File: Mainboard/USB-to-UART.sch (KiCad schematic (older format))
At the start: 8 parts, among them U9 CH340B

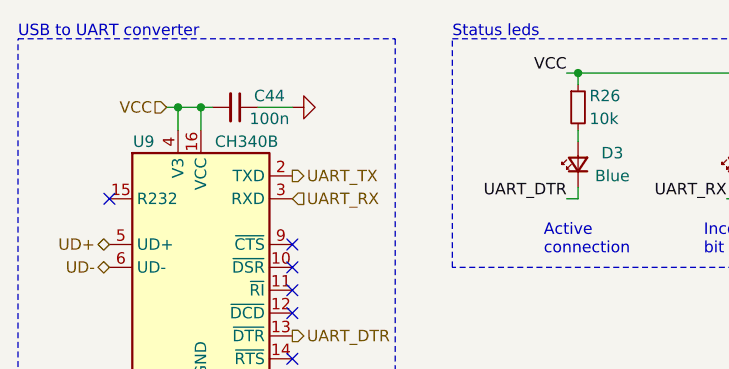
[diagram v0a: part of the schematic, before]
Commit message: Before testing CH340B and VCHG
Cleaned up amp lay-out a bit in the meanwhile
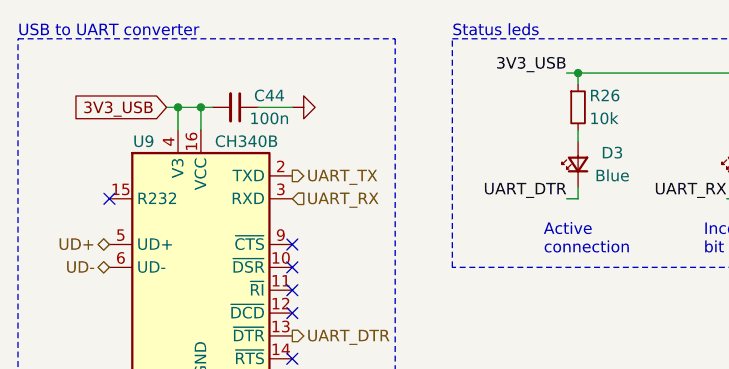
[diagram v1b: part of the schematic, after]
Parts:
- C44: Manufacturer Walsin -> Murata; Partnumber 0603B104J500CT -> GCM188L81H104KA57D
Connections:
- net VCC renamed 3V3_USB
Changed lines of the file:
@@
 $Descr A4 11693 8268
 encoding utf-8
-Sheet 2 9
+Sheet 10 11
 Title "4x38W amp with DSP and BT"
-Date "2021-11-08"
+Date "2021-11-19"
 Rev "0.2"
 Comp "ZOUDIO"
@@
 F 2 "Capacitor_SMD:C_0603_1608Metric" H 4950 3100 50  0001 C CNN
 F 3 "~" H 4950 3100 50  0001 C CNN
-F 4 "Walsin" H 4950 3100 50  0001 C CNN "Manufacturer"
-F 5 "0603B104J500CT" H 4950 3100 50  0001 C CNN "Partnumber"
+F 4 "Murata" H 4950 3100 50  0001 C CNN "Manufacturer"
+F 5 "GCM188L81H104KA57D" H 4950 3100 50  0001 C CNN "Partnumber"
 	1    4950 3100
 	0    1    1    0
@@
 Wire Wire Line
 	4650 3100 4700 3100
-Text HLabel 4650 3100 0    50   Input ~ 0
-VCC
 Connection ~ 4700 3100
 Wire Wire Line
 	6450 2950 6400 2950
-Text Label 6400 2950 2    50   ~ 0
-VCC
 Text Label 6400 3500 2    50   ~ 0
 UART_DTR
@@
 	8100 3800 5900 3800
 $Comp
-L power:GND #PWR?
+L power:GND #PWR0162
 U 1 1 61ADB0CE
 P 4800 4450
-F 0 "#PWR?" H 4800 4200 50  0001 C CNN
+F 0 "#PWR0162" H 4800 4200 50  0001 C CNN
 F 1 "GND" H 4800 4300 50  0000 C CNN
 F 2 "" H 4800 4450 50  0001 C CNN
@@
 	1    0    0    -1
 $EndComp
+Text GLabel 4650 3100 0    50   Input ~ 0
+3V3_USB
+Text Label 6400 2950 2    50   ~ 0
+3V3_USB
 $EndSCHEMATC

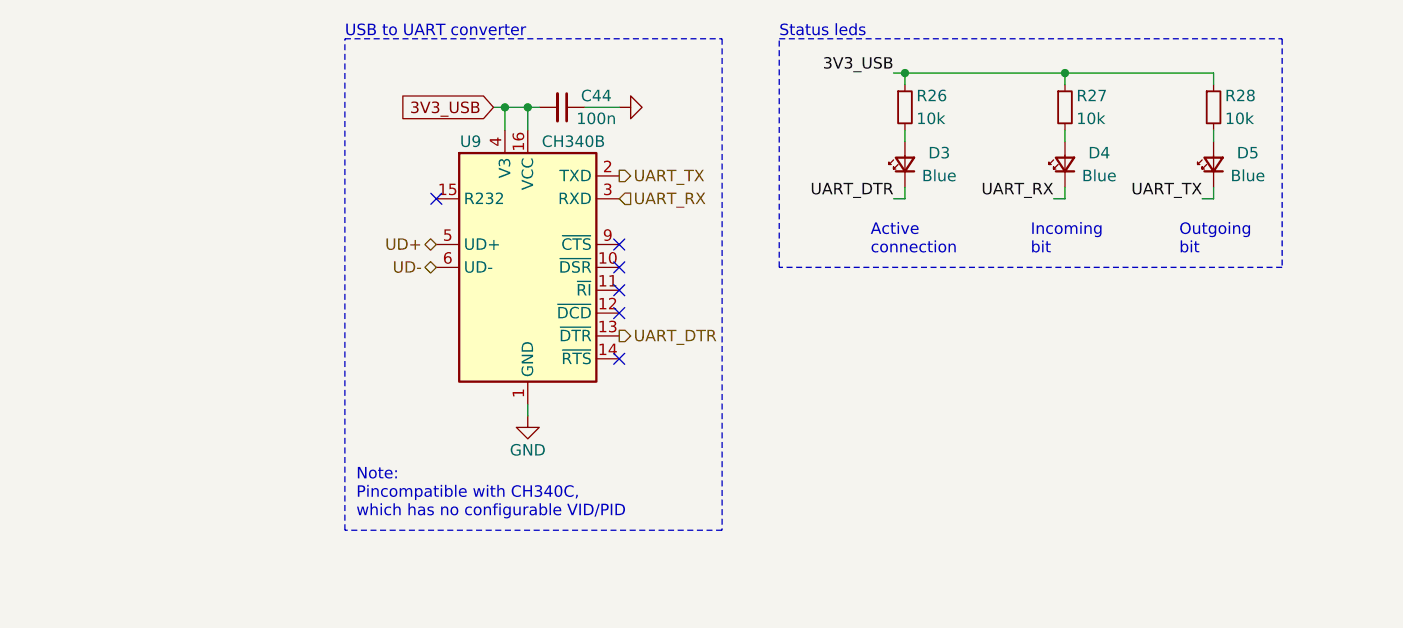
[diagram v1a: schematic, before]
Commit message: Result after weekend of lay-out
Pretty far, just neats to be cleaned up for production.
Does not pass DRC yet.
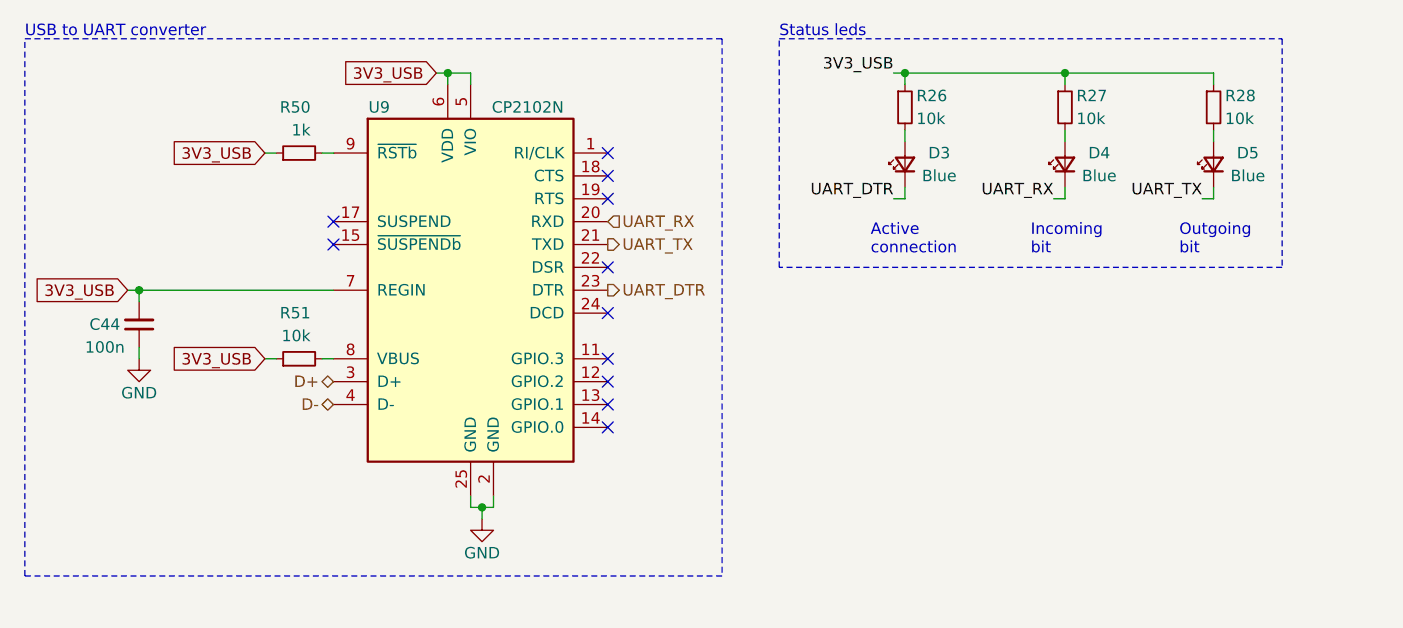
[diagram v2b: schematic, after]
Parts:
- removed U9: CH340B, Package_SO:SOIC-16_3.9x9.9mm_P1.27mm, symbol Interface_USB:CH340C
- added R50: 1k, Resistor_SMD:R_0603_1608Metric, symbol Device:R_Small
- added R51: 10k, Resistor_SMD:R_0603_1608Metric, symbol Device:R_Small
- added U9: CP2102N, Package_DFN_QFN:QFN-24-1EP_4x4mm_P0.5mm_EP2.6x2.6mm, symbol Interface_USB:CP2102N-A01-GQFN24
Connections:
- net 3V3_USB: now also R50.1, R51.1, U9.5 (VIO), U9.6 (VDD), U9.7 (REGIN)
- net GND: now also U9.2 (GND), U9.25 (GND)
- net UART_DTR: now also U9.23 (DTR)
- net UART_RX: now also U9.20 (RXD)
- net UART_TX: now also U9.21 (TXD)
- new net: R51.2, U9.8 (VBUS)
- new net: R50.2, U9.9 (~RSTb)
- new net D+: U9.3 (D+)
- new net D-: U9.4 (D-)
- no-connect marks 6 -> 11
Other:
- note removed: "Note:\nPincompatible with CH340C,\nwhich has no configurable VID/PID"
- moved on the sheet: C44
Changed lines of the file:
@@
 Comment4 ""
 $EndDescr
-$Comp
-L power:GND #PWR?
-U 1 1 5FD85D4B
-P 5200 3100
-AR Path="/5FD85D4B" Ref="#PWR?"  Part="1"
-AR Path="/5FD15AD6/5FD85D4B" Ref="#PWR?"  Part="1"
-AR Path="/5FBDE62F/5FD85D4B" Ref="#PWR?"  Part="1"
-AR Path="/5FD81784/5FD85D4B" Ref="#PWR?"  Part="1"
-AR Path="/5FCDB1AE/5FD85D4B" Ref="#PWR?"  Part="1"
-AR Path="/5FF9E05B/5FD85D4B" Ref="#PWR?"  Part="1"
-AR Path="/60A7E145/5FD85D4B" Ref="#PWR0186"  Part="1"
-F 0 "#PWR0186" H 5200 2850 50  0001 C CNN
-F 1 "GND" H 5205 2927 50  0001 C CNN
-F 2 "" H 5200 3100 50  0001 C CNN
-F 3 "" H 5200 3100 50  0001 C CNN
-	1    5200 3100
-	0    -1   -1   0
-$EndComp
-Text HLabel 5200 4100 2    50   Output ~ 0
+Text HLabel 5150 3900 2    50   Output ~ 0
 UART_DTR
 Wire Notes Line
-	5650 4950 4000 4950
-Wire Notes Line
-	4000 4950 4000 2800
-Text HLabel 4400 3700 0    50   BiDi ~ 0
-UD+
-Text HLabel 4400 3800 0    50   BiDi ~ 0
-UD-
+	5650 5150 2600 5150
+Wire Notes Line
+	2600 5150 2600 2800
+Text HLabel 3950 4300 0    50   BiDi ~ 0
+D+
+Text HLabel 3950 4400 0    50   BiDi ~ 0
+D-
 $Comp
 L Device:C_Small C?
 U 1 1 5FD85D40
-P 4950 3100
+P 3100 4050
 AR Path="/5FD85D40" Ref="C?"  Part="1"
 AR Path="/5FCC1D27/5FD85D40" Ref="C?"  Part="1"
@@
 AR Path="/5FF9E05B/5FD85D40" Ref="C?"  Part="1"
 AR Path="/60A7E145/5FD85D40" Ref="C44"  Part="1"
-F 0 "C44" V 4900 3250 50  0000 C CNN
-F 1 "100n" V 5000 3250 50  0000 C CNN
-F 2 "Capacitor_SMD:C_0603_1608Metric" H 4950 3100 50  0001 C CNN
-F 3 "~" H 4950 3100 50  0001 C CNN
-F 4 "Murata" H 4950 3100 50  0001 C CNN "Manufacturer"
-F 5 "GCM188L81H104KA57D" H 4950 3100 50  0001 C CNN "Partnumber"
-	1    4950 3100
-	0    1    1    0
-$EndComp
-Wire Wire Line
-	5200 3100 5050 3100
-Wire Wire Line
-	4850 3100 4800 3100
-Wire Wire Line
-	4700 3200 4700 3100
-Wire Wire Line
-	4700 3100 4800 3100
-Connection ~ 4800 3100
-Wire Wire Line
-	4800 3100 4800 3200
-NoConn ~ 4400 3500
-NoConn ~ 5200 3700
-NoConn ~ 5200 3800
-NoConn ~ 5200 3900
-NoConn ~ 5200 4000
-NoConn ~ 5200 4200
-Wire Wire Line
-	4800 4400 4800 4450
-$Comp
-L Interface_USB:CH340C U9
-U 1 1 60B2C7AB
-P 4800 3800
-F 0 "U9" H 4550 4350 50  0000 C CNN
-F 1 "CH340B" H 5000 4350 50  0000 C CNN
-F 2 "Package_SO:SOIC-16_3.9x9.9mm_P1.27mm" H 4850 3250 50  0001 L CNN
-F 3 "~" H 4450 4600 50  0001 C CNN
-	1    4800 3800
-	1    0    0    -1
-$EndComp
-Text Notes 4050 4900 0    50   ~ 0
-Note:\nPincompatible with CH340C,\nwhich has no configurable VID/PID
-Text Notes 4000 2800 0    50   ~ 0
+F 0 "C44" H 2950 4050 50  0000 C CNN
+F 1 "100n" H 2950 4150 50  0000 C CNN
+F 2 "Capacitor_SMD:C_0603_1608Metric" H 3100 4050 50  0001 C CNN
+F 3 "~" H 3100 4050 50  0001 C CNN
+F 4 "Murata" H 3100 4050 50  0001 C CNN "Manufacturer"
+F 5 "GCM188L81H104KA57D" H 3100 4050 50  0001 C CNN "Partnumber"
+	1    3100 4050
+	1    0    0    1
+$EndComp
+Text Notes 2600 2800 0    50   ~ 0
 USB to UART converter
-Wire Notes Line
-	4000 2800 5650 2800
-Text HLabel 5200 3500 2    50   Input ~ 0
+Text HLabel 5150 3600 2    50   Input ~ 0
 UART_RX
-Text HLabel 5200 3400 2    50   Output ~ 0
+Text HLabel 5150 3700 2    50   Output ~ 0
 UART_TX
 Wire Notes Line
-	5650 2800 5650 4950
+	5650 2800 5650 5150
 Text Notes 5900 2800 0    50   ~ 0
 Status leds
@@
 $EndComp
 Wire Wire Line
-	4650 3100 4700 3100
-Connection ~ 4700 3100
-Wire Wire Line
 	6450 2950 6400 2950
 Text Label 6400 3500 2    50   ~ 0
@@
 Wire Notes Line
 	8100 3800 5900 3800
+Text Label 6400 2950 2    50   ~ 0
+3V3_USB
+$Comp
+L Interface_USB:CP2102N-A01-GQFN24 U9
+U 1 1 61A39051
+P 4550 3900
+F 0 "U9" H 4150 4700 50  0000 C CNN
+F 1 "CP2102N" H 4800 4700 50  0000 C CNN
+F 2 "Package_DFN_QFN:QFN-24-1EP_4x4mm_P0.5mm_EP2.6x2.6mm" H 5000 3100 50  0001 L CNN
+F 3 "https://www.silabs.com/documents/public/data-sheets/cp2102n-datasheet.pdf" H 4600 2850 50  0001 C CNN
+	1    4550 3900
+	1    0    0    -1
+$EndComp
 $Comp
 L power:GND #PWR0162
-U 1 1 61ADB0CE
-P 4800 4450
-F 0 "#PWR0162" H 4800 4200 50  0001 C CNN
-F 1 "GND" H 4800 4300 50  0000 C CNN
-F 2 "" H 4800 4450 50  0001 C CNN
-F 3 "" H 4800 4450 50  0001 C CNN
-	1    4800 4450
-	1    0    0    -1
-$EndComp
-Text GLabel 4650 3100 0    50   Input ~ 0
-3V3_USB
-Text Label 6400 2950 2    50   ~ 0
-3V3_USB
+U 1 1 61A3E5C2
+P 4600 4900
+F 0 "#PWR0162" H 4600 4650 50  0001 C CNN
+F 1 "GND" H 4600 4750 50  0000 C CNN
+F 2 "" H 4600 4900 50  0001 C CNN
+F 3 "" H 4600 4900 50  0001 C CNN
+	1    4600 4900
+	1    0    0    -1
+$EndComp
+Wire Wire Line
+	4550 4800 4550 4850
+Wire Wire Line
+	4550 4850 4600 4850
+Wire Wire Line
+	4650 4850 4650 4800
+Wire Wire Line
+	4600 4850 4600 4900
+Connection ~ 4600 4850
+Wire Wire Line
+	4600 4850 4650 4850
+Wire Wire Line
+	4450 3000 4450 2950
+Wire Wire Line
+	4550 2950 4550 3000
+Text GLabel 4400 2950 0    50   Input ~ 0
+3V3_USB
+Wire Wire Line
+	4400 2950 4450 2950
+Connection ~ 4450 2950
+Wire Wire Line
+	4450 2950 4550 2950
+Text GLabel 3650 3300 0    50   Input ~ 0
+3V3_USB
+$Comp
+L Device:R_Small R?
+U 1 1 61A416D4
+P 3800 3300
+AR Path="/5FBDE745/61A416D4" Ref="R?"  Part="1"
+AR Path="/5FBDE62F/61A416D4" Ref="R?"  Part="1"
+AR Path="/5FD81784/61A416D4" Ref="R?"  Part="1"
+AR Path="/5FCDB1AE/61A416D4" Ref="R?"  Part="1"
+AR Path="/5FF9E05B/61A416D4" Ref="R?"  Part="1"
+AR Path="/60A7E145/61A416D4" Ref="R50"  Part="1"
+F 0 "R50" V 4000 3250 50  0000 L CNN
+F 1 "1k" V 3900 3250 50  0000 L CNN
+F 2 "Resistor_SMD:R_0603_1608Metric" H 3800 3300 50  0001 C CNN
+F 3 "~" H 3800 3300 50  0001 C CNN
+F 4 "Uni-royal" H 3800 3300 50  0001 C CNN "Manufacturer"
+F 5 "0603WAF1002T5E" H 3800 3300 50  0001 C CNN "Partnumber"
+	1    3800 3300
+	0    -1   -1   0
+$EndComp
+Wire Wire Line
+	3650 3300 3700 3300
+Wire Wire Line
+	3900 3300 3950 3300
+Text GLabel 3650 4200 0    50   Input ~ 0
+3V3_USB
+$Comp
+L Device:R_Small R?
+U 1 1 61A46BEA
+P 3800 4200
+AR Path="/5FBDE745/61A46BEA" Ref="R?"  Part="1"
+AR Path="/5FBDE62F/61A46BEA" Ref="R?"  Part="1"
+AR Path="/5FD81784/61A46BEA" Ref="R?"  Part="1"
+AR Path="/5FCDB1AE/61A46BEA" Ref="R?"  Part="1"
+AR Path="/5FF9E05B/61A46BEA" Ref="R?"  Part="1"
+AR Path="/60A7E145/61A46BEA" Ref="R51"  Part="1"
+F 0 "R51" V 4000 4150 50  0000 L CNN
+F 1 "10k" V 3900 4150 50  0000 L CNN
+F 2 "Resistor_SMD:R_0603_1608Metric" H 3800 4200 50  0001 C CNN
+F 3 "~" H 3800 4200 50  0001 C CNN
+F 4 "Uni-royal" H 3800 4200 50  0001 C CNN "Manufacturer"
+F 5 "0603WAF1002T5E" H 3800 4200 50  0001 C CNN "Partnumber"
+	1    3800 4200
+	0    -1   -1   0
+$EndComp
+Wire Wire Line
+	3700 4200 3650 4200
+Wire Wire Line
+	3900 4200 3950 4200
+Text GLabel 3050 3900 0    50   Input ~ 0
+3V3_USB
+Wire Wire Line
+	3050 3900 3100 3900
+Wire Wire Line
+	3100 3900 3100 3950
+Wire Wire Line
+	3100 3900 3950 3900
+Connection ~ 3100 3900
+$Comp
+L power:GND #PWR0175
+U 1 1 61A4CA6C
+P 3100 4200
+F 0 "#PWR0175" H 3100 3950 50  0001 C CNN
+F 1 "GND" H 3100 4050 50  0000 C CNN
+F 2 "" H 3100 4200 50  0001 C CNN
+F 3 "" H 3100 4200 50  0001 C CNN
+	1    3100 4200
+	1    0    0    -1
+$EndComp
+Wire Wire Line
+	3100 4150 3100 4200
+NoConn ~ 5150 3300
+NoConn ~ 5150 3400
+NoConn ~ 5150 3500
+NoConn ~ 5150 3800
+NoConn ~ 5150 4000
+NoConn ~ 5150 4200
+NoConn ~ 5150 4300
+NoConn ~ 5150 4400
+NoConn ~ 5150 4500
+Wire Notes Line
+	2600 2800 5650 2800
+NoConn ~ 3950 3600
+NoConn ~ 3950 3700
 $EndSCHEMATC

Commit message: Mainboard: Version 1.0
Still need to clean up 3D models and BoM list,
but gerberexport-ready and ready to order.
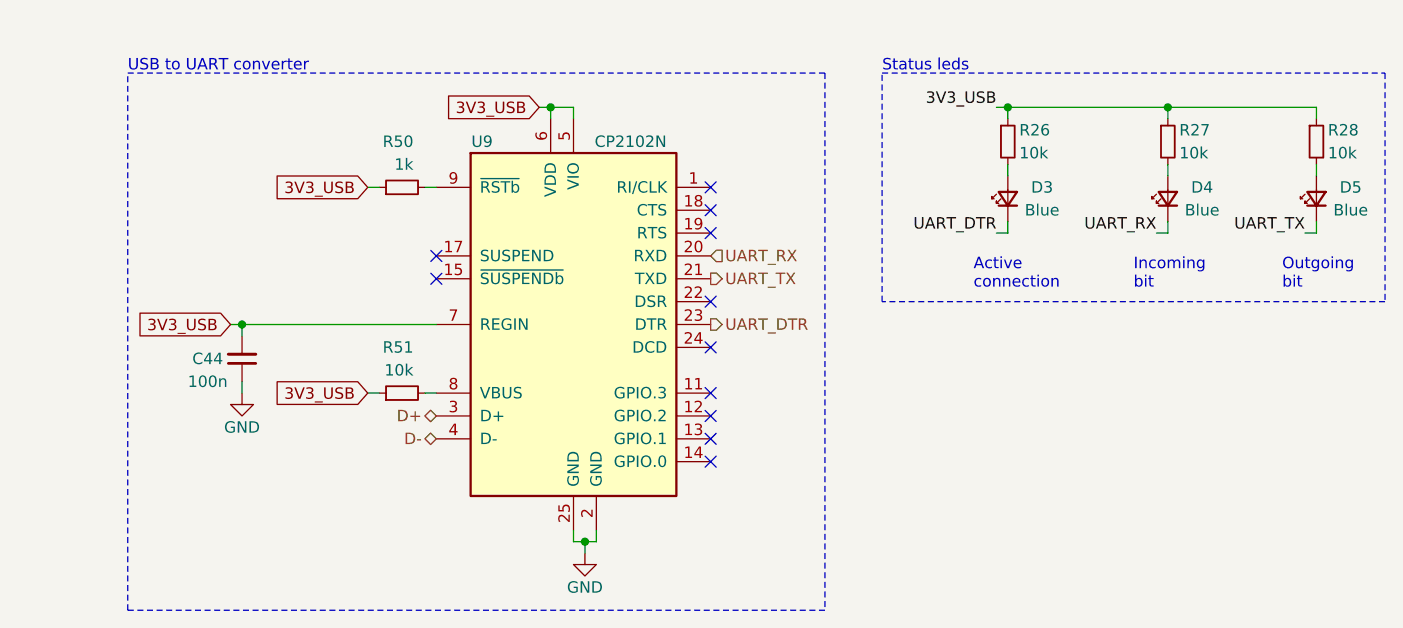
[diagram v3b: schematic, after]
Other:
- moved on the sheet: C44, D3, D4, D5, R26, R27, R28, R50, R51, U9

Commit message: Clean up schematic for BoM export
- Change 22u 0805's (amp decoupling) to 15u
- Change 680n 0805's (part of output filter) to 470n
- Change C1 (amp bulk cap) from 820u to 1000u
- Add BoM.ini for KiBom export and
- Complete fields needed for KiBom (Manufacturer and partnumber)
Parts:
- D3, D4, D5: Manufacturer Orient -> Wurth; Partnumber ORH-B36G -> 150060BS75000
- R26, R27, R28, R51: Manufacturer Uni-royal -> Yageo; Partnumber 0603WAF1002T5E -> RC0603FR-0710KL
- R50: Manufacturer Uni-royal -> Yageo; Partnumber 0603WAF1002T5E -> RC0603FR-071KL
- U9: Manufacturer (none) -> Silicon Labs; Partnumber (none) -> CP2102N-A02-GQFN24
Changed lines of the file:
@@
 F 2 "LED_SMD:LED_0603_1608Metric" V 6900 3500 50  0001 C CNN
 F 3 "~" V 6900 3500 50  0001 C CNN
-F 4 "Orient" H 6900 3500 50  0001 C CNN "Manufacturer"
-F 5 "ORH-B36G" H 6900 3500 50  0001 C CNN "Partnumber"
+F 4 "Wurth" H 6900 3500 50  0001 C CNN "Manufacturer"
+F 5 "150060BS75000" H 6900 3500 50  0001 C CNN "Partnumber"
 	1    6900 3500
 	0    -1   -1   0
@@
 F 2 "Resistor_SMD:R_0603_1608Metric" H 6900 3250 50  0001 C CNN
 F 3 "~" H 6900 3250 50  0001 C CNN
-F 4 "Uni-royal" H 6900 3250 50  0001 C CNN "Manufacturer"
-F 5 "0603WAF1002T5E" H 6900 3250 50  0001 C CNN "Partnumber"
+F 4 "Yageo" H 6900 3250 50  0001 C CNN "Manufacturer"
+F 5 "RC0603FR-0710KL" H 6900 3250 50  0001 C CNN "Partnumber"
 	1    6900 3250
 	1    0    0    -1
@@
 F 2 "LED_SMD:LED_0603_1608Metric" V 7600 3500 50  0001 C CNN
 F 3 "~" V 7600 3500 50  0001 C CNN
-F 4 "Orient" H 7600 3500 50  0001 C CNN "Manufacturer"
-F 5 "ORH-B36G" H 7600 3500 50  0001 C CNN "Partnumber"
+F 4 "Wurth" H 7600 3500 50  0001 C CNN "Manufacturer"
+F 5 "150060BS75000" H 7600 3500 50  0001 C CNN "Partnumber"
 	1    7600 3500
 	0    -1   -1   0
@@
 F 2 "Resistor_SMD:R_0603_1608Metric" H 7600 3250 50  0001 C CNN
 F 3 "~" H 7600 3250 50  0001 C CNN
-F 4 "Uni-royal" H 7600 3250 50  0001 C CNN "Manufacturer"
-F 5 "0603WAF1002T5E" H 7600 3250 50  0001 C CNN "Partnumber"
+F 4 "Yageo" H 7600 3250 50  0001 C CNN "Manufacturer"
+F 5 "RC0603FR-0710KL" H 7600 3250 50  0001 C CNN "Partnumber"
 	1    7600 3250
 	1    0    0    -1
@@
 F 2 "LED_SMD:LED_0603_1608Metric" V 8250 3500 50  0001 C CNN
 F 3 "~" V 8250 3500 50  0001 C CNN
-F 4 "Orient" H 8250 3500 50  0001 C CNN "Manufacturer"
-F 5 "ORH-B36G" H 8250 3500 50  0001 C CNN "Partnumber"
+F 4 "Wurth" H 8250 3500 50  0001 C CNN "Manufacturer"
+F 5 "150060BS75000" H 8250 3500 50  0001 C CNN "Partnumber"
 	1    8250 3500
 	0    -1   -1   0
@@
 F 2 "Resistor_SMD:R_0603_1608Metric" H 8250 3250 50  0001 C CNN
 F 3 "~" H 8250 3250 50  0001 C CNN
-F 4 "Uni-royal" H 8250 3250 50  0001 C CNN "Manufacturer"
-F 5 "0603WAF1002T5E" H 8250 3250 50  0001 C CNN "Partnumber"
+F 4 "Yageo" H 8250 3250 50  0001 C CNN "Manufacturer"
+F 5 "RC0603FR-0710KL" H 8250 3250 50  0001 C CNN "Partnumber"
 	1    8250 3250
 	1    0    0    -1
@@
 F 2 "Package_DFN_QFN:QFN-24-1EP_4x4mm_P0.5mm_EP2.6x2.6mm" H 5450 3250 50  0001 L CNN
 F 3 "https://www.silabs.com/documents/public/data-sheets/cp2102n-datasheet.pdf" H 5050 3000 50  0001 C CNN
+F 4 "Silicon Labs" H 5000 4050 50  0001 C CNN "Manufacturer"
+F 5 "CP2102N-A02-GQFN24" H 5000 4050 50  0001 C CNN "Partnumber"
 	1    5000 4050
 	1    0    0    -1
@@
 F 2 "Resistor_SMD:R_0603_1608Metric" H 4250 3450 50  0001 C CNN
 F 3 "~" H 4250 3450 50  0001 C CNN
-F 4 "Uni-royal" H 4250 3450 50  0001 C CNN "Manufacturer"
-F 5 "0603WAF1002T5E" H 4250 3450 50  0001 C CNN "Partnumber"
+F 4 "Yageo" H 4250 3450 50  0001 C CNN "Manufacturer"
+F 5 "RC0603FR-071KL" H 4250 3450 50  0001 C CNN "Partnumber"
 	1    4250 3450
 	0    -1   -1   0
@@
 F 2 "Resistor_SMD:R_0603_1608Metric" H 4250 4350 50  0001 C CNN
 F 3 "~" H 4250 4350 50  0001 C CNN
-F 4 "Uni-royal" H 4250 4350 50  0001 C CNN "Manufacturer"
-F 5 "0603WAF1002T5E" H 4250 4350 50  0001 C CNN "Partnumber"
+F 4 "Yageo" H 4250 4350 50  0001 C CNN "Manufacturer"
+F 5 "RC0603FR-0710KL" H 4250 4350 50  0001 C CNN "Partnumber"
 	1    4250 4350
 	0    -1   -1   0
